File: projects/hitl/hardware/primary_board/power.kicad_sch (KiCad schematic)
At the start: 19 parts, among them J20 CONN_01X03, U1 PCA9517, U9 LT3045

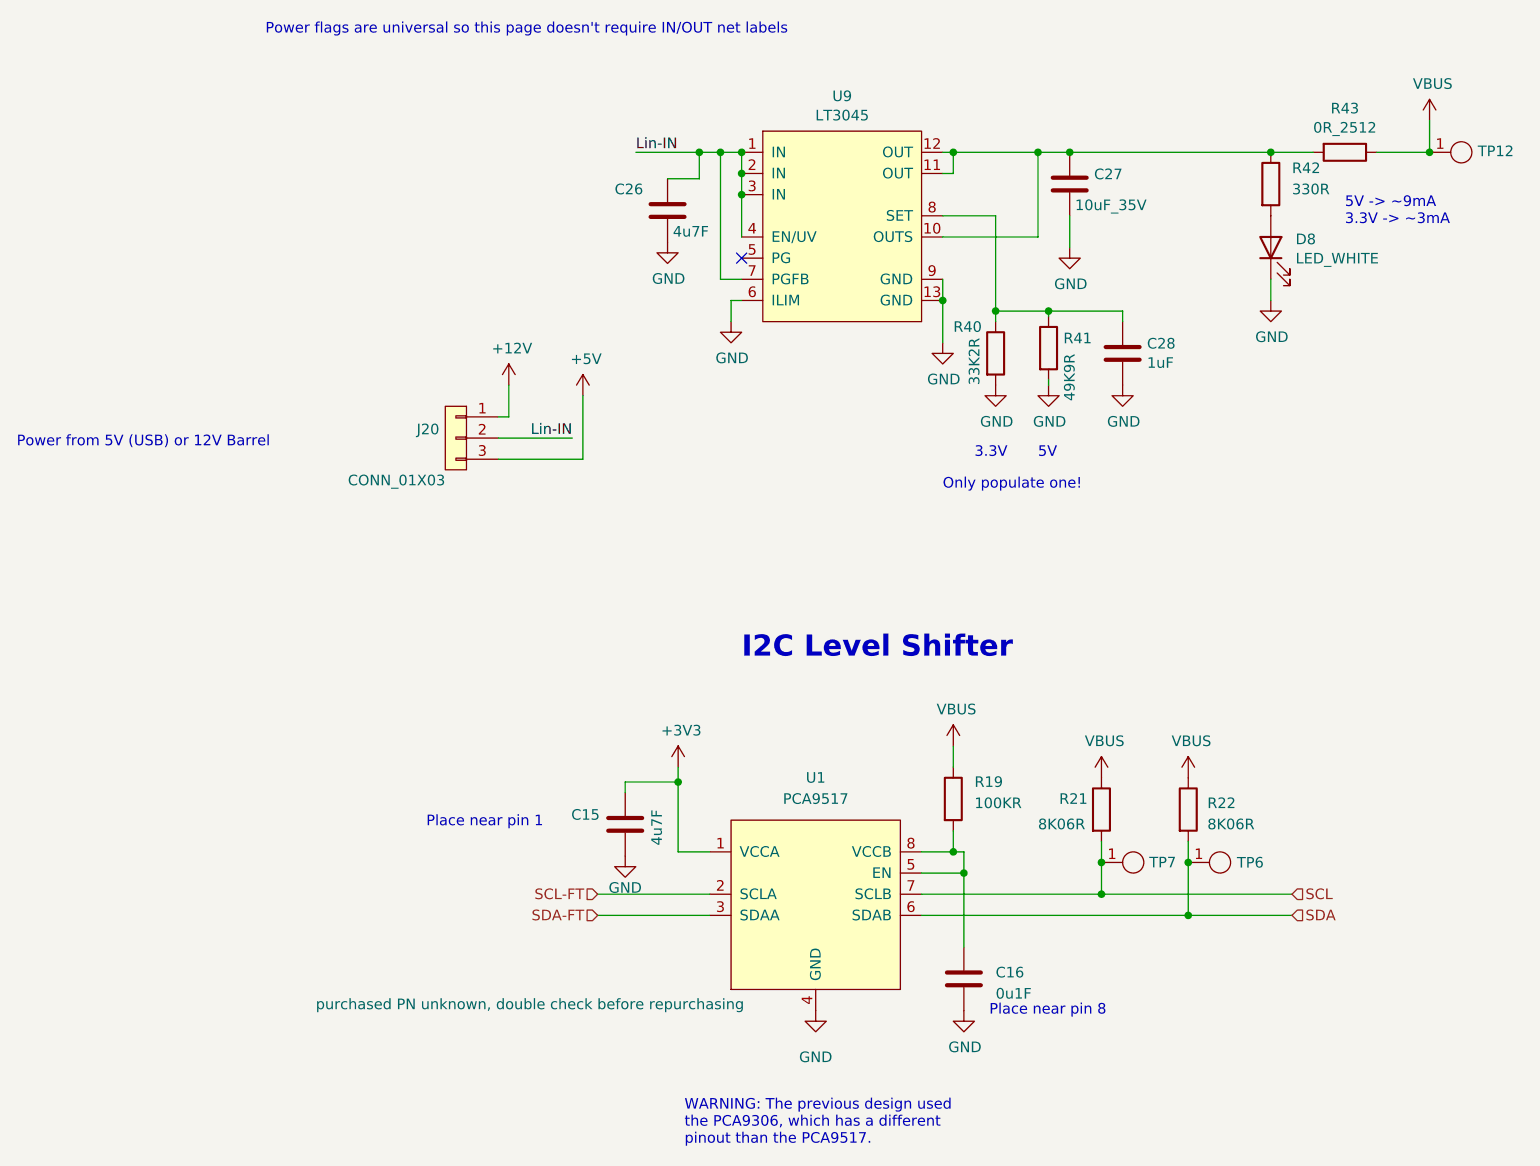
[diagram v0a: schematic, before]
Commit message: Fixes to HitL hardware from testing
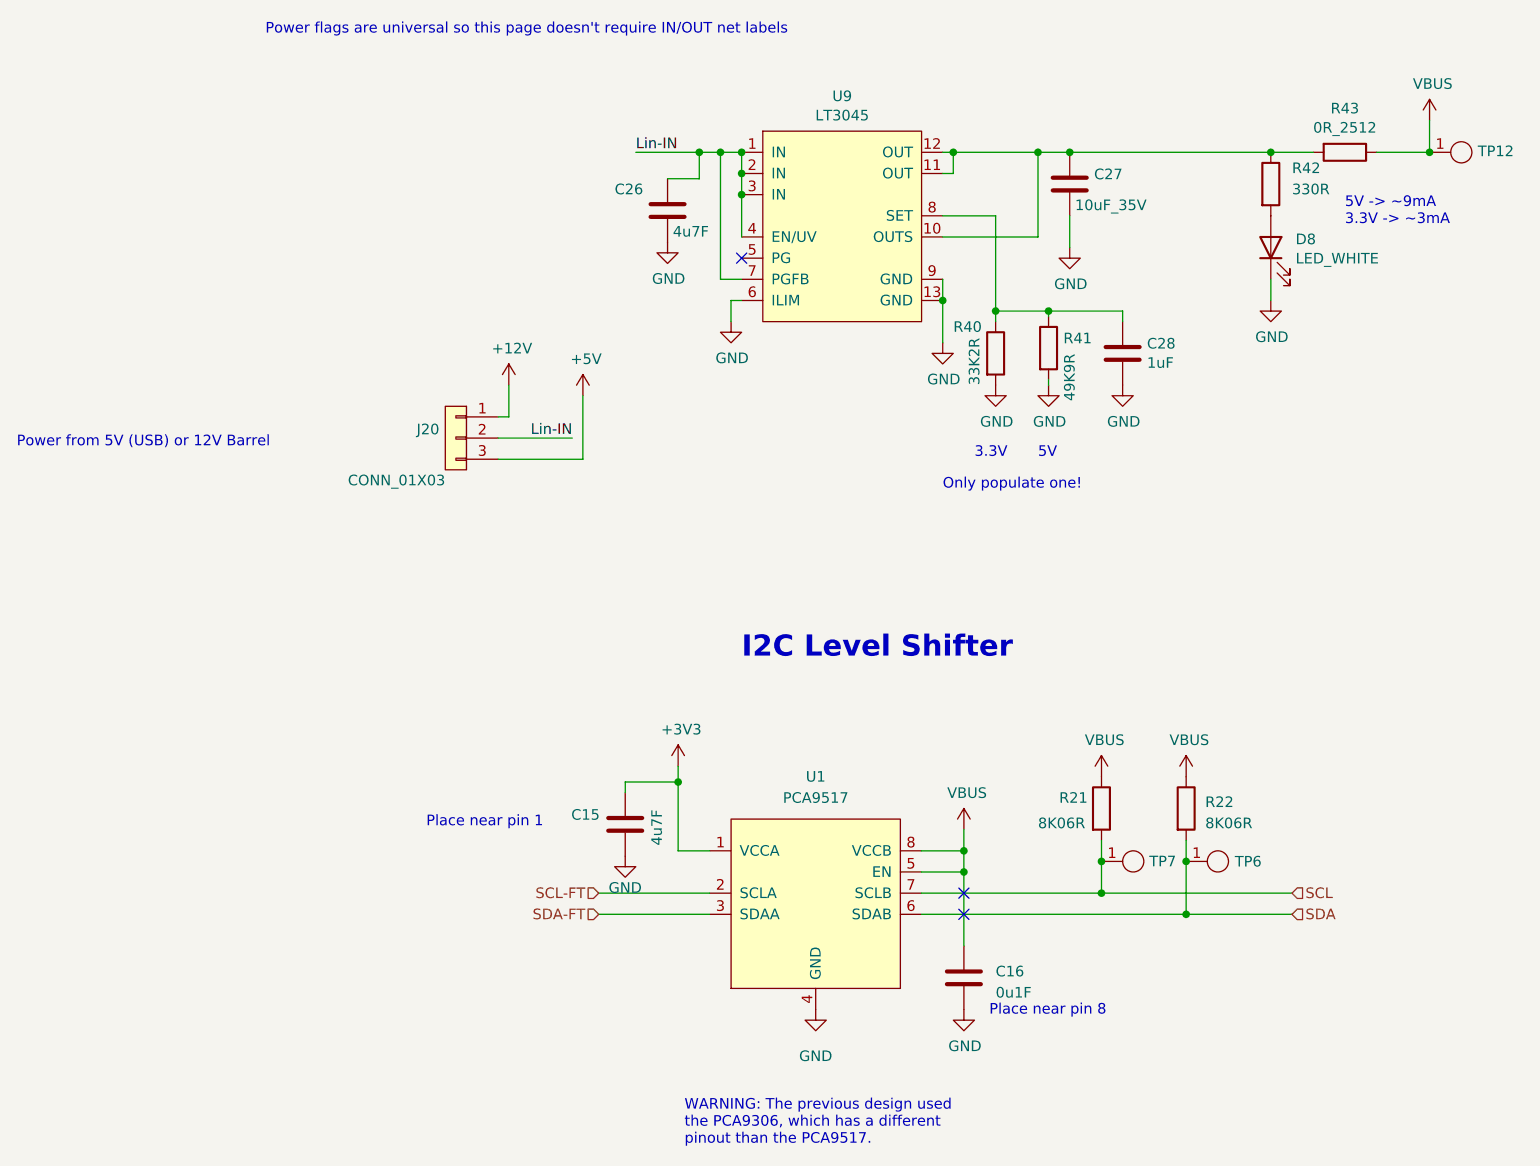
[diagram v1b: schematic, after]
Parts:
- removed R19: 100KR, OEM:R_0603, symbol OEM:100KR
- U1: MPN PCA9306DCUTG4 -> PCA9517; NOTE purchased PN unknown, double check before repurchasing -> (none)
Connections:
- net VBUS: now also C16.1, U1.5 (EN), U1.8 (VCCB)
- no-connect marks 1 -> 3
